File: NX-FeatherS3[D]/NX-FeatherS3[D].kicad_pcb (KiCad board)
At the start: 4 copper layers, 22.9 x 50.8 mm, 17 parts, among them J1 USB_C_Receptacle_USB2.0_14P, J2 Right-Side, J3 Left-Side, J4 Conn_01x02_Pin, J5 Conn_01x02_Pin, U1 ESP32-S3, U10 BNO085, U11 BGS12WN6E6327, U2 NCP167BMX330TBG, U3 MAX17048G_T10, U5 NCP167BMX330TBG, U6 W25Q128JVSIQ, U7 LY68L6400SLIT, U8 BQ25170DSGR, U9 MAX98357A

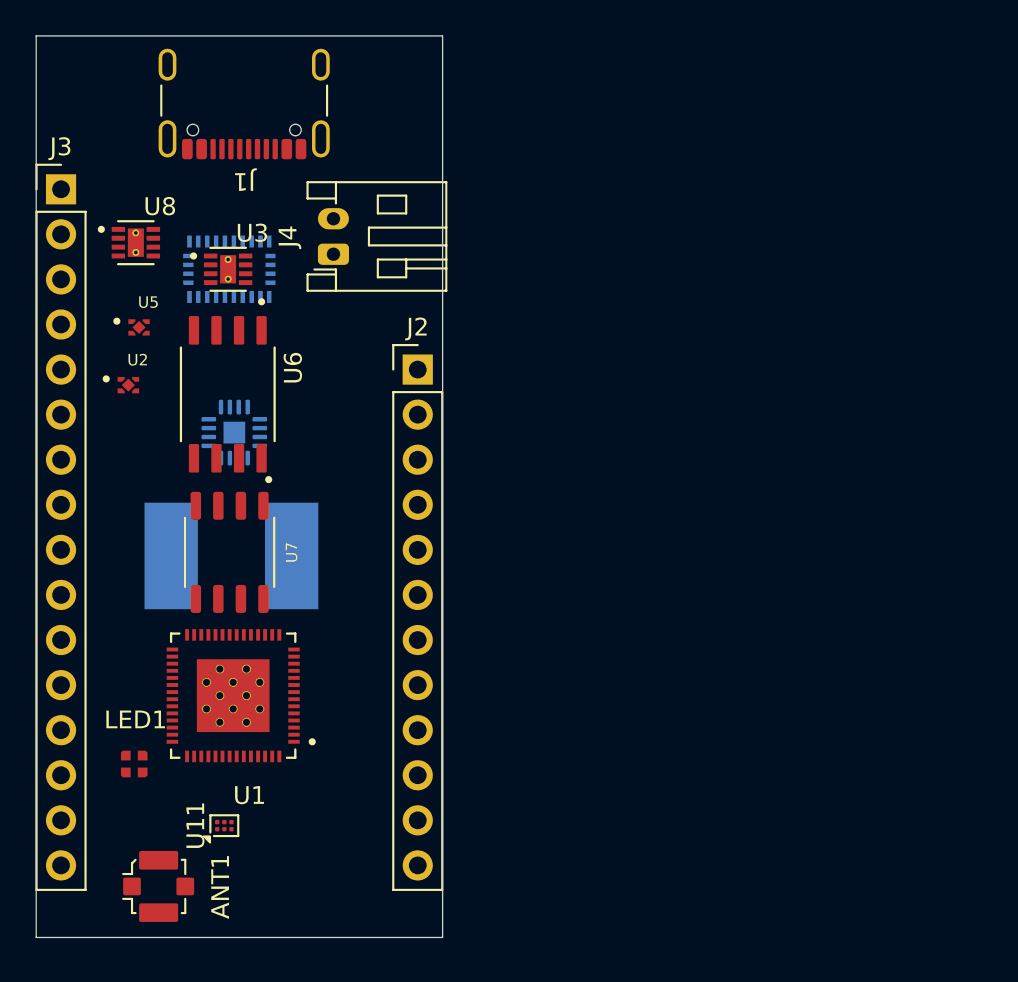
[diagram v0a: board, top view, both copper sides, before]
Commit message: Added v1p0, updated Version
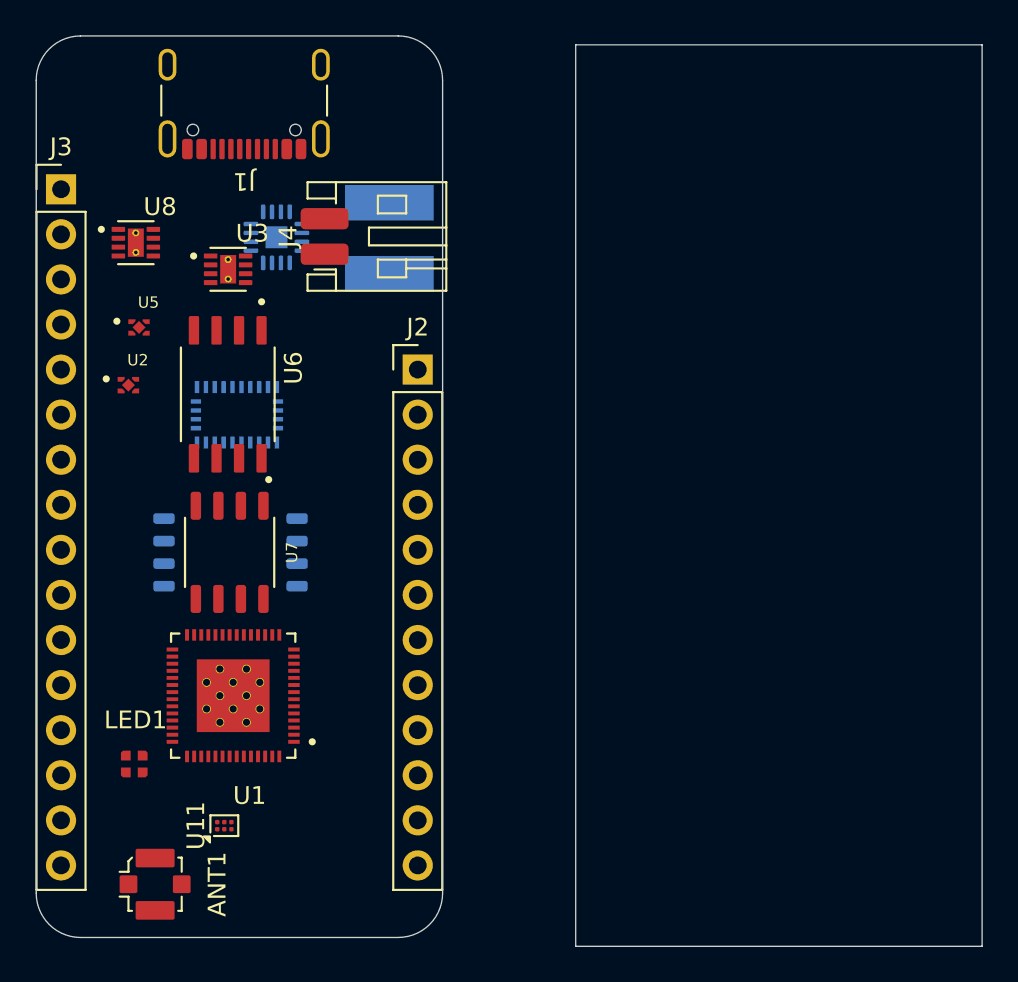
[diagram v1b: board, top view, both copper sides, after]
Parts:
- added F1: ZDSD32GLGEAG, Package_LGA:LGA-8_8x6.2mm_P1.27mm, B.Cu at (110.5, 68.4)
- moved J5 19.9 mm to (119.5, 50.7), turned to 90 degrees
- moved U9 11.3 mm to (113.1, 50.6)
- moved U10 8.21 mm to (110.9, 60.6)
- moved ANT1 0.24 mm to (106.3, 87.1)
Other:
- board size 22.9 x 50.8 mm -> 53.3 x 51.3 mm
